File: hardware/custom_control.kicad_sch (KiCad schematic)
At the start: 6 parts, among them Q1 2N7002, Q2 2N7002

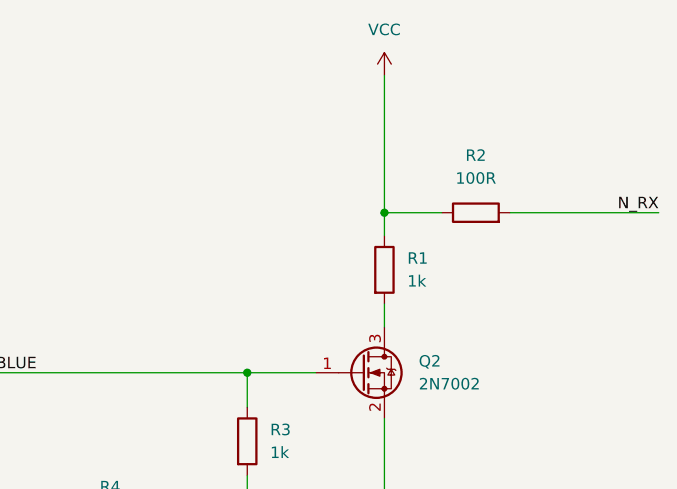
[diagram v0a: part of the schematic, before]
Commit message: Updated HW design for connecting to the bus
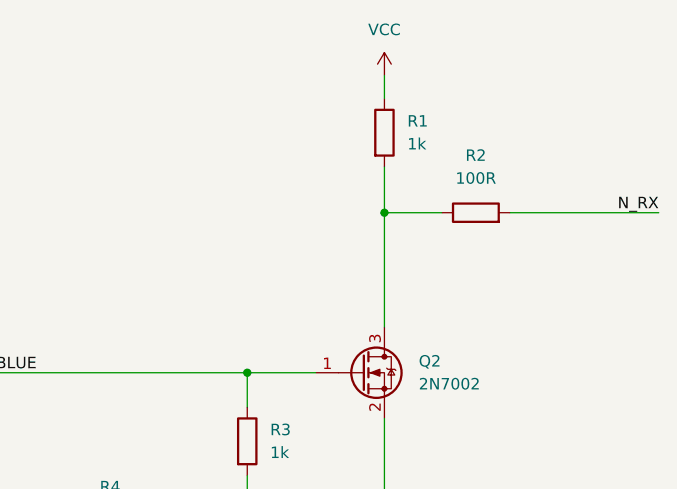
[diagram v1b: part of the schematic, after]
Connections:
- net VCC: no longer R2.1
- net at Q2.3 (D), R1.2: now also R2.1
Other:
- moved on the sheet: R1
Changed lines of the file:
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@@
 	(wire
 		(pts
-			(xy 72.39 54.61) (xy 72.39 57.15)
+			(xy 72.39 39.37) (xy 72.39 44.45)
 		)
 		(stroke
@@
 	(wire
 		(pts
-			(xy 72.39 29.21) (xy 72.39 44.45)
-		)
-		(stroke
-			(width 0)
-			(type default)
-		)
-	)
-	(wire
-		(pts
-			(xy 72.39 44.45) (xy 72.39 46.99)
+			(xy 72.39 29.21) (xy 72.39 31.75)
+		)
+		(stroke
+			(width 0)
+			(type default)
+		)
+	)
+	(wire
+		(pts
+			(xy 72.39 44.45) (xy 72.39 57.15)
 		)
 		(stroke
@@
 	(symbol
 		(lib_id "Device:R")
-		(at 72.39 50.8 0)
+		(at 72.39 35.56 0)
 		(unit 1)
 		(exclude_from_sim no)
@@
 		(fields_autoplaced yes)
 		(property "Reference" "R1"
-			(at 74.93 49.5299 0)
+			(at 74.93 34.2899 0)
 			(effects
 				(font
@@
 		)
 		(property "Value" "1k"
-			(at 74.93 52.0699 0)
+			(at 74.93 36.8299 0)
 			(effects
 				(font
@@
 		)
 		(property "Footprint" ""
-			(at 70.612 50.8 90)
+			(at 70.612 35.56 90)
 			(effects
 				(font
@@
 		)
 		(property "Datasheet" "~"
-			(at 72.39 50.8 0)
+			(at 72.39 35.56 0)
 			(effects
 				(font
@@
 		)
 		(property "Description" "Resistor"
-			(at 72.39 50.8 0)
-			(effects
-				(font
+			(at 72.39 35.56 0)
+			(effects
+				(font

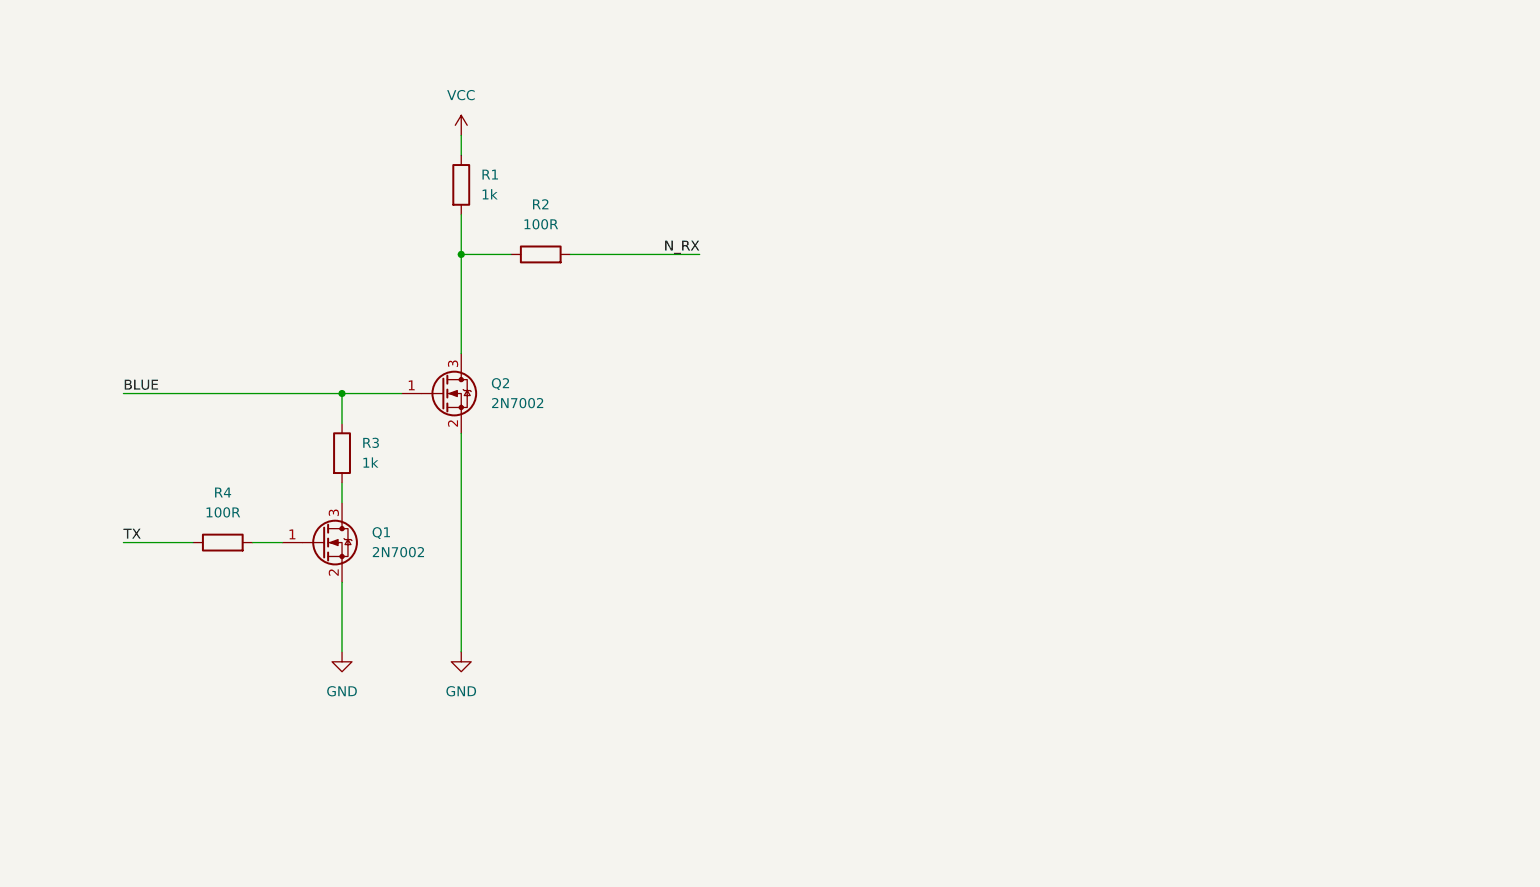
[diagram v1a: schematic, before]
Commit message: Updated schematics to make it more clear
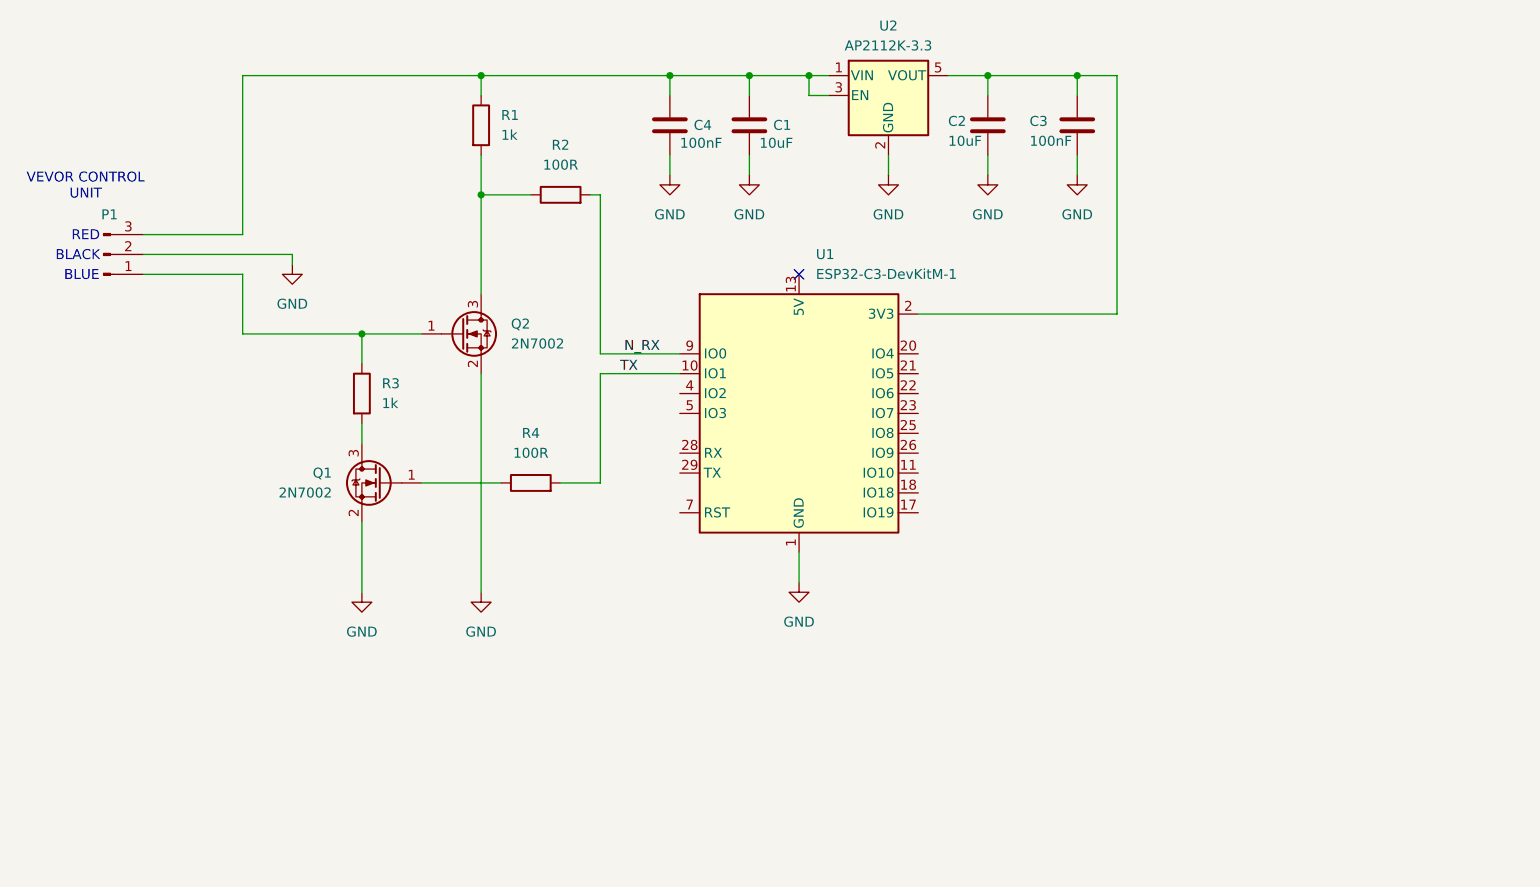
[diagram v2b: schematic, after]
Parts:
- added C1, C2: 10uF, symbol Device:C
- added C3, C4: 100nF, symbol Device:C
- added P1: Conn_01x03_Pin, symbol Connector:Conn_01x03_Pin
- added U1: ESP32-C3-DevKitM-1, RF_Module:ESP32-C3-DevKitM-1, symbol RF_Module:ESP32-C3-DevKitM-1
- added U2: AP2112K-3.3, Package_TO_SOT_SMD:SOT-23-5, symbol Regulator_Linear:AP2112K-3.3
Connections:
- net GND: now also C1.2, C2.2, C3.2, C4.2, P1.2 (Pin_2), U1.1 (GND), U1.12 (GND), U1.15 (GND), U1.16 (GND), U1.19 (GND), U1.24 (GND), U1.27 (GND), U1.30 (GND), U1.6 (GND), U1.8 (GND), U2.2 (GND)
- net N_RX: now also U1.9 (IO0)
- net TX: now also R4.2, U1.10 (IO1); no longer R4.1
- net at Q1.1 (G): now also R4.1; no longer R4.2
- net BLUE: no longer names the net of Q2.1 (G), R3.1
- net BLUE: now also P1.1 (Pin_1)
- net VCC: no longer names the net of R1.1
- net VCC: now also C1.1, C4.1, P1.3 (Pin_3), U2.1 (VIN), U2.3 (EN)
- new net: U1.13 (5V), U1.14 (5V)
- new net: C2.1, C3.1, U1.2 (3V3), U1.3 (3V3), U2.5 (VOUT)
- no-connect marks 0 -> 1
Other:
- note added: "BLACK"
- note added: "BLUE"
- note added: "RED"
- note added: "VEVOR CONTROL UNIT"
- moved on the sheet: Q1, Q2, R1, R2, R3, R4

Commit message: Fixed issue in schematics made in last commit.  Changed readme to be more clear.
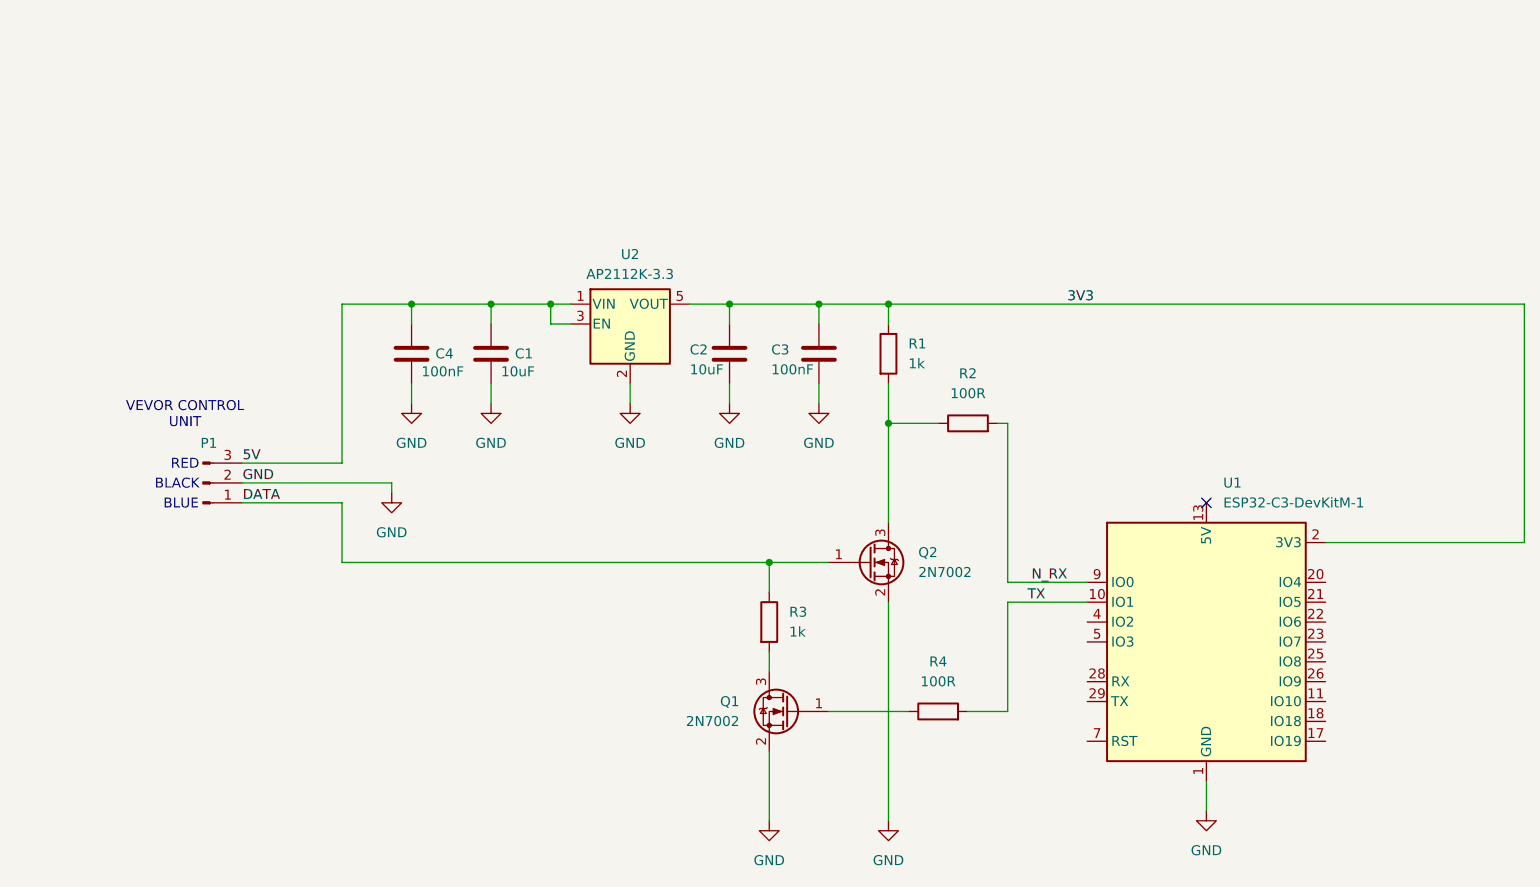
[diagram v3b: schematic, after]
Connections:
- net DATA: now reaches P1.1 (Pin_1), Q2.1 (G), R3.1
- net 3V3: now reaches C2.1, C3.1, U1.2 (3V3), U1.3 (3V3), U2.5 (VOUT)
- net 3V3: now also R1.1
- net 5V: now reaches C1.1, C4.1, P1.3 (Pin_3), U2.1 (VIN), U2.3 (EN)
- net 5V: no longer R1.1
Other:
- moved on the sheet: C1, C2, C3, C4, P1, Q1, Q2, R1, R2, R3, R4, U1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

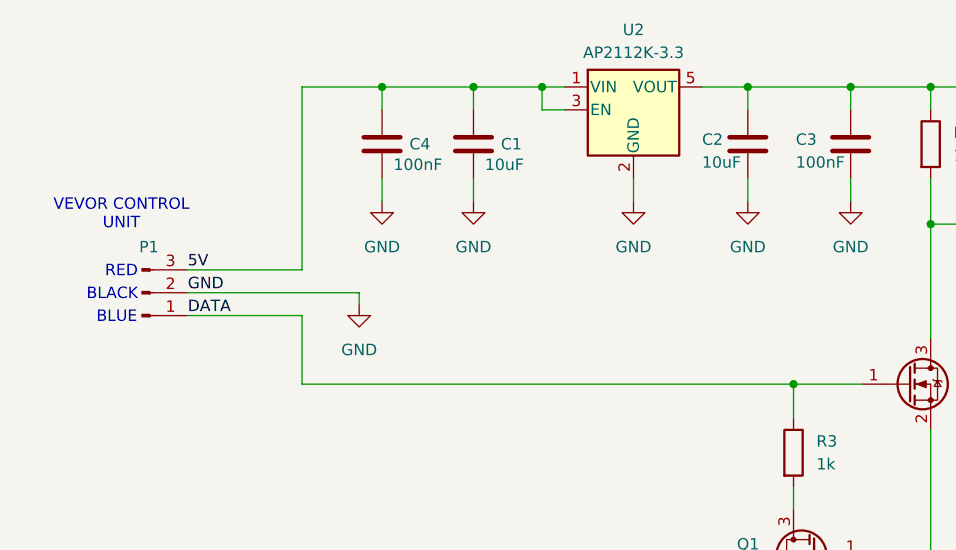
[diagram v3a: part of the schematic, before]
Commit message: Added missing pull-up in schematics
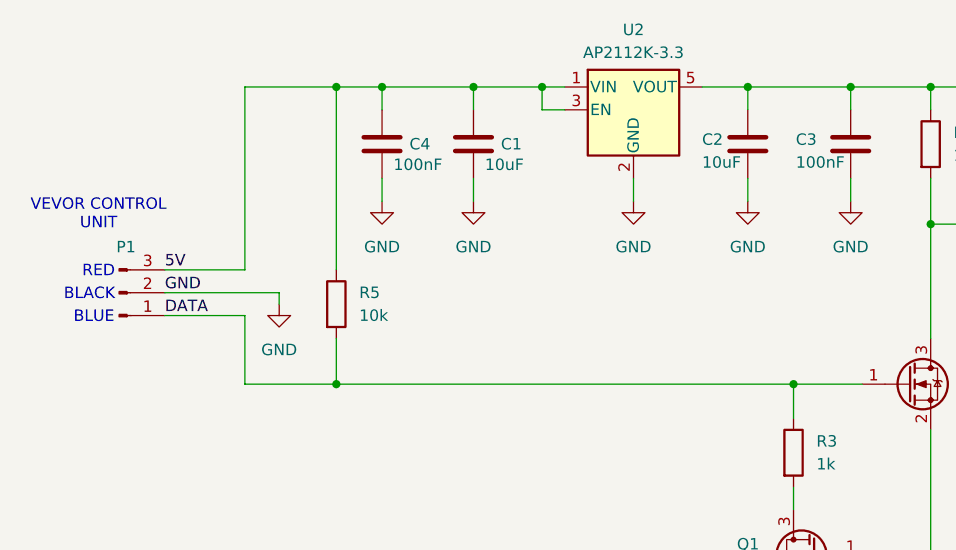
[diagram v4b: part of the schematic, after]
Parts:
- added R5: 10k, symbol Device:R
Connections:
- net 5V: now also R5.1
- net DATA: now also R5.2
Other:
- moved on the sheet: P1
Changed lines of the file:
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@@
 	(text "RED"
 		(exclude_from_sim no)
-		(at 37.084 71.374 0)
+		(at 34.544 71.374 0)
 		(effects
 			(font
@@
 	(text "VEVOR CONTROL\nUNIT"
 		(exclude_from_sim no)
-		(at 37.084 65.024 0)
+		(at 34.544 65.024 0)
 		(effects
 			(font
@@
 	(text "BLACK"
 		(exclude_from_sim no)
-		(at 36.068 73.914 0)
+		(at 33.528 73.914 0)
 		(effects
 			(font
@@
 	(text "BLUE"
 		(exclude_from_sim no)
-		(at 36.576 76.454 0)
+		(at 34.036 76.454 0)
 		(effects
 			(font
@@
 	)
 	(junction
+		(at 60.96 50.8)
+		(diameter 0)
+		(color 0 0 0 0)
+	)
+	(junction
 		(at 111.76 83.82)
 		(diameter 0)
@@
 	)
 	(junction
+		(at 60.96 83.82)
+		(diameter 0)
+		(color 0 0 0 0)
+	)
+	(junction
 		(at 127 50.8)
 		(diameter 0)
@@
 	(wire
 		(pts
+			(xy 60.96 78.74) (xy 60.96 83.82)
+		)
+		(stroke
+			(width 0)
+			(type default)
+		)
+	)
+	(wire
+		(pts
 			(xy 167.64 111.76) (xy 167.64 115.57)
 		)
@@
 	(wire
 		(pts
-			(xy 44.45 71.12) (xy 57.15 71.12)
+			(xy 60.96 50.8) (xy 60.96 71.12)
+		)
+		(stroke
+			(width 0)
+			(type default)
+		)
+	)
+	(wire
+		(pts
+			(xy 41.91 71.12) (xy 50.8 71.12)
 		)
 		(stroke
@@
 	(wire
 		(pts
-			(xy 57.15 76.2) (xy 44.45 76.2)
+			(xy 50.8 76.2) (xy 41.91 76.2)
 		)
 		(stroke
@@
 	(wire
 		(pts
-			(xy 63.5 73.66) (xy 63.5 74.93)
+			(xy 54.61 73.66) (xy 54.61 74.93)
 		)
 		(stroke
@@
 	(wire
 		(pts
-			(xy 57.15 50.8) (xy 66.04 50.8)
+			(xy 50.8 50.8) (xy 60.96 50.8)
 		)
 		(stroke
@@
 	(wire
 		(pts
-			(xy 44.45 73.66) (xy 63.5 73.66)
+			(xy 41.91 73.66) (xy 54.61 73.66)
 		)
 		(stroke
@@
 	(wire
 		(pts
+			(xy 60.96 83.82) (xy 111.76 83.82)
+		)
+		(stroke
+			(width 0)
+			(type default)
+		)
+	)
+	(wire
+		(pts
 			(xy 127 50.8) (xy 208.28 50.8)
 		)
@@
 	(wire
 		(pts
-			(xy 57.15 76.2) (xy 57.15 83.82)
+			(xy 50.8 76.2) (xy 50.8 83.82)
 		)
 		(stroke
@@
 	(wire
 		(pts
-			(xy 57.15 83.82) (xy 111.76 83.82)
+			(xy 50.8 83.82) (xy 60.96 83.82)
 		)
 		(stroke
@@
 	(wire
 		(pts
-			(xy 57.15 71.12) (xy 57.15 50.8)
+			(xy 50.8 71.12) (xy 50.8 50.8)
 		)
 		(stroke
@@
 		(pts
 			(xy 101.6 50.8) (xy 106.68 50.8)
+		)
+		(stroke
+			(width 0)
+			(type default)
+		)
+	)
+	(wire
+		(pts
+			(xy 60.96 50.8) (xy 66.04 50.8)
 		)
 		(stroke
@@
 	)
 	(label "GND"
-		(at 44.45 73.66 0)
+		(at 41.91 73.66 0)
 		(effects
 			(font
@@
 	)
 	(label "DATA"
-		(at 44.45 76.2 0)
+		(at 41.91 76.2 0)
 		(effects
 			(font
@@
 	)
 	(label "5V"
-		(at 44.45 71.12 0)
+		(at 41.91 71.12 0)
 		(effects
 			(font
@@
 	(symbol
 		(lib_id "power:GND")
-		(at 63.5 74.93 0)
+		(at 54.61 74.93 0)
 		(unit 1)
 		(exclude_from_sim no)
@@
 		(fields_autoplaced yes)
 		(property "Reference" "#PWR012"
-			(at 63.5 81.28 0)
+			(at 54.61 81.28 0)
 			(effects
 				(font
@@
 		)
 		(property "Value" "GND"
-			(at 63.5 80.01 0)
+			(at 54.61 80.01 0)
 			(effects
 				(font
@@
 		)
 		(property "Footprint" ""
-			(at 63.5 74.93 0)
+			(at 54.61 74.93 0)
 			(effects
 				(font
@@
 		)
 		(property "Datasheet" ""
-			(at 63.5 74.93 0)
+			(at 54.61 74.93 0)
 			(effects
 				(font
@@
 		)
 		(property "Description" "Power symbol creates a global label with name \"GND\" , ground"
-			(at 63.5 74.93 0)
+			(at 54.61 74.93 0)
 			(effects
 				(font
@@
 	(symbol
 		(lib_id "Connector:Conn_01x03_Pin")
-		(at 39.37 73.66 0)
+		(at 36.83 73.66 0)
 		(mirror x)
 		(unit 1)
@@
 		(dnp no)
 		(property "Reference" "P1"
-			(at 40.132 68.58 0)
+			(at 37.592 68.58 0)
 			(effects
 				(font
@@
 		)
 		(property "Value" "Conn_01x03_Pin"
-			(at 40.005 78.74 0)
+			(at 37.465 78.74 0)
 			(effects
 				(font
@@
 		)
 		(property "Footprint" ""
-			(at 39.37 73.66 0)
+			(at 36.83 73.66 0)
 			(effects
 				(font
@@
 		)
 		(property "Datasheet" "~"
-			(at 39.37 73.66 0)
+			(at 36.83 73.66 0)
 			(effects
 				(font
@@
 		)
 		(property "Description" "Generic connector, single row, 01x03, script generated"
-			(at 39.37 73.66 0)
+			(at 36.83 73.66 0)
 			(effects
 				(font
@@
 					(unit 1)
 				)
+			)
+		)
+	)
+	(symbol
+		(lib_id "Device:R")
+		(at 60.96 74.93 0)
+		(unit 1)
+		(exclude_from_sim no)
+		(in_bom yes)
+		(on_board yes)
+		(dnp no)
+		(fields_autoplaced yes)
+		(property "Reference" "R5"
+			(at 63.5 73.6599 0)
+			(effects
+				(font
+					(size 1.27 1.27)
+				)
+				(justify left)
+			)
+		)
+		(property "Value" "10k"
+			(at 63.5 76.1999 0)
+			(effects
+				(font
+					(size 1.27 1.27)
+				)
+				(justify left)
+			)
+		)
+		(property "Footprint" ""
+			(at 59.182 74.93 90)
+			(effects
+				(font
+					(size 1.27 1.27)
+				)
+				(hide yes)
+			)
+		)
+		(property "Datasheet" "~"
+			(at 60.96 74.93 0)
+			(effects
+				(font
+					(size 1.27 1.27)
+				)
+				(hide yes)
+			)
+		)
+		(property "Description" "Resistor"
+			(at 60.96 74.93 0)
+			(effects
+				(font
+					(size 1.27 1.27)
+				)
+				(hide yes)
+			)
+		)
+		(pin "2"
+		)
+		(pin "1"
+		)
+		(instances
+			(project "custom_control"
+				(path "/cf7080a1-edbe-4f6f-aaf1-39d8a05512e2"
+					(reference "R5")
+					(unit 1)
+				)
